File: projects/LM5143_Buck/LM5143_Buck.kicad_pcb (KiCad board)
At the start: 4 copper layers, 83 x 55 mm, 91 parts, among them J1 Bat In, J2 24V Out, J3 I2C Socket, J4 I2C Socket, Q1 IGC025S08S1, Q2 IGC025S08S1, Q3 IGC025S08S1, Q4 IGC025S08S1, SW1 Addr_Switch, SW2 Addr_Switch, U2 TLV74033, U3 INA226

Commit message: New Schematic
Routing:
- net VOUT: track 104.0 -> 0.00 mm, vias 6 -> 0
- net Net-(J3-Pin_4): track 88.7 -> 0.00 mm, vias 3 -> 0
- net Net-(J3-Pin_3): track 87.4 -> 0.00 mm, vias 3 -> 0
- net +24V: track 57.0 -> 0.00 mm, vias 57 -> 0
- net +3.3V: track 55.0 -> 0.00 mm, vias 2 -> 0
- net +5V: track 49.8 -> 0.00 mm, vias 3 -> 0
- net GNDA: track 46.5 -> 0.00 mm, vias 1 -> 0
- net Net-(U3-A1): track 35.5 -> 0.00 mm, vias 1 -> 0
- net Net-(U1-CS1): track 33.1 -> 0.00 mm, vias 2 -> 0
- net Net-(U1-CS2): track 32.9 -> 0.00 mm, vias 2 -> 0
- net /~{Alert}: track 32.1 -> 0.00 mm, vias 3 -> 0
- net PGND2: track 22.9 -> 0.00 mm, vias 2 -> 0
- net PGND1: track 19.2 -> 0.00 mm, vias 1 -> 0
- net Net-(D5-A): track 18.2 -> 0.00 mm, vias 2 -> 0
- net Net-(D3-A): track 16.4 -> 0.00 mm, vias 2 -> 0
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
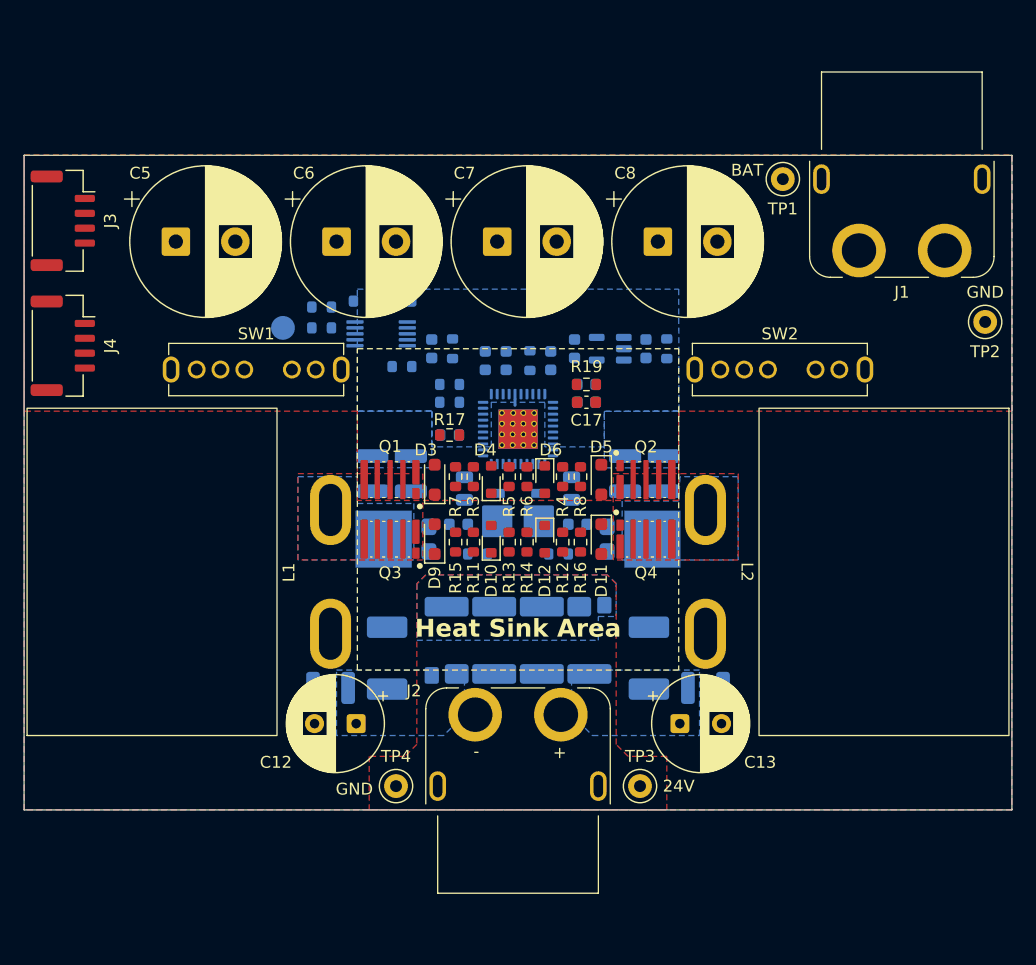
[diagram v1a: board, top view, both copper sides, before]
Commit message: Schematic update and partial routing
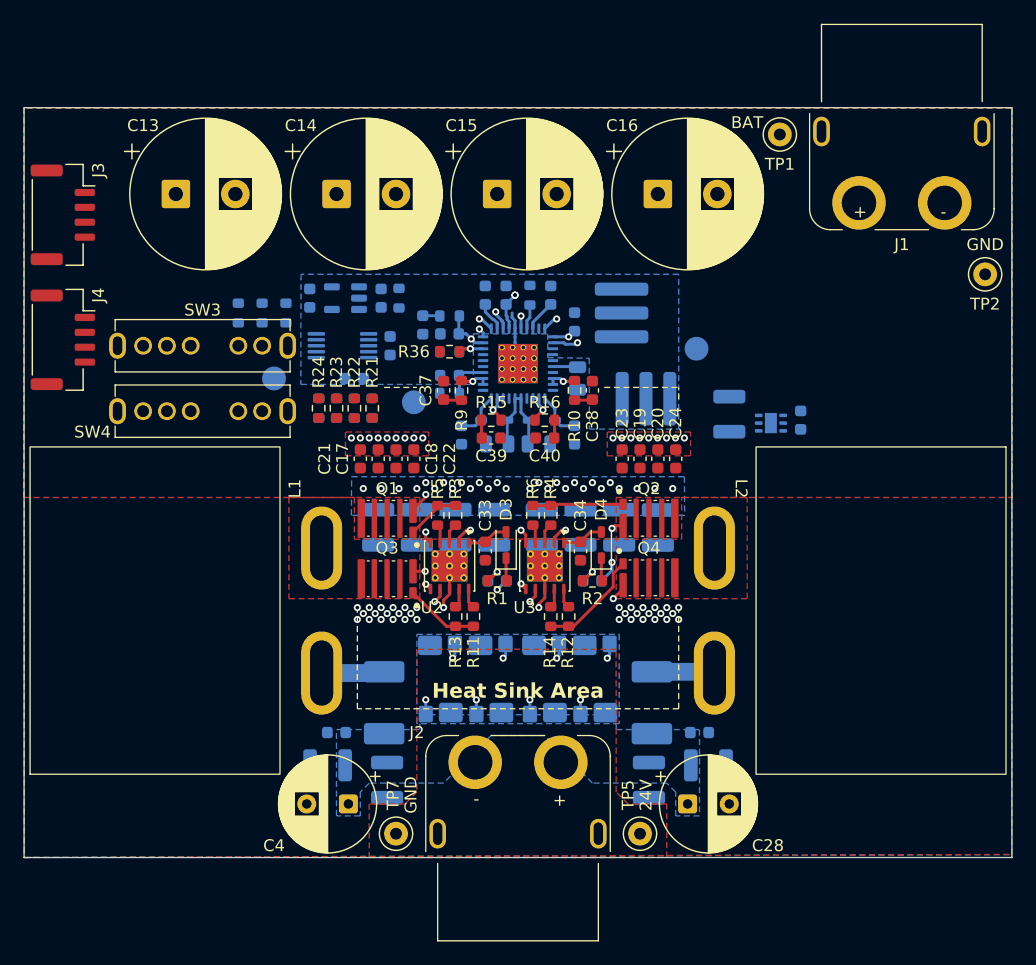
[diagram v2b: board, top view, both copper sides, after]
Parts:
- removed the C13 at (153.6, 130.2)
- removed the C14 at (155.8, 127.2)
- removed the C15 at (135.0, 113.5)
- removed the C16 at (145.0, 113.5)
- removed D10, D12, D6: PLZ5V1C, footprints:D_MicroSMF
- removed D11, D9: CUS10S30, Diode_SMD:D_SOD-323_HandSoldering
- removed D13: B18W1NG--20C000114U1930, LED_SMD:LED_0603_1608Metric
- removed D7, D8: MBR15H120PC-AU, Package_TO_SOT_SMD:TO-277A
- added C27: 100nF, Capacitor_SMD:C_0603_1608Metric, B.Cu at (155.2, 131.0)
- added C28: 100uF, Capacitor_THT:CP_Radial_D8.0mm_P3.50mm, F.Cu at (154.2, 137.0)
- added C29: 2.2uF, Capacitor_SMD:C_0805_2012Metric, B.Cu at (138.2, 106.8)
- added C30: 2.2uF, Capacitor_SMD:C_0805_2012Metric, B.Cu at (141.8, 106.8)
- added C31: 100nF, Capacitor_SMD:C_0603_1608Metric, B.Cu at (138.2, 118.2)
- added C32: 100nF, Capacitor_SMD:C_0603_1608Metric, B.Cu at (146.2, 118.2)
- added C33: 1uF, Capacitor_SMD:C_0603_1608Metric, F.Cu at (137.2, 115.8)
- added C34: 1uF, Capacitor_SMD:C_0603_1608Metric, F.Cu at (145.2, 115.8)
- added C35: 100nF, Capacitor_SMD:C_0603_1608Metric, B.Cu at (135.2, 106.0)
- added C36: 100nF, Capacitor_SMD:C_0603_1608Metric, B.Cu at (144.8, 106.0)
- added C37: 22pF, Capacitor_SMD:C_0603_1608Metric, F.Cu at (133.8, 102.2)
- added C38: 22pF, Capacitor_SMD:C_0603_1608Metric, F.Cu at (146.2, 102.2)
- added C39: 22pF, Capacitor_SMD:C_0603_1608Metric, F.Cu at (137.8, 106.2)
- added C40: 22pF, Capacitor_SMD:C_0603_1608Metric, F.Cu at (142.2, 106.2)
- added C41: 2.2uF, Capacitor_SMD:C_0805_2012Metric, B.Cu at (145.0, 101.2)
- added C42: 5.6nF, Capacitor_SMD:C_0603_1608Metric, B.Cu at (132.0, 96.8)
- added C43: 1uF, Capacitor_SMD:C_0603_1608Metric, B.Cu at (128.5, 94.5)
- added C44: 1uF, Capacitor_SMD:C_0603_1608Metric, B.Cu at (122.5, 94.5)
- added C45: 120pF, Capacitor_SMD:C_0603_1608Metric, B.Cu at (134.2, 97.5)
- added C46: 100nF, Capacitor_SMD:C_0603_1608Metric, B.Cu at (144.8, 96.5)
- added C47: 470nF, Capacitor_SMD:C_0603_1608Metric, B.Cu at (137.2, 94.2)
- added C48: 470nF, Capacitor_SMD:C_0603_1608Metric, B.Cu at (139.0, 94.2)
- added C49: 10nF, Capacitor_SMD:C_0603_1608Metric, B.Cu at (142.8, 94.2)
- added C5: 4.7uF, Capacitor_SMD:C_1210_3225Metric, B.Cu at (128.2, 113.8)
- added C50: 1uF, Capacitor_SMD:C_0603_1608Metric, B.Cu at (163.8, 104.8)
- added C51: 10uF, Capacitor_SMD:C_1210_3225Metric, B.Cu at (157.8, 104.2)
- added C52: 100nF, Capacitor_SMD:C_0603_1608Metric, B.Cu at (129.2, 98.5)
- added C53: 1uF, Capacitor_SMD:C_0603_1608Metric, B.Cu at (126.2, 101.2)
- added C6: 4.7uF, Capacitor_SMD:C_1210_3225Metric, B.Cu at (131.5, 113.8)
- added C7: 4.7uF, Capacitor_SMD:C_1210_3225Metric, B.Cu at (134.8, 113.8)
- added C8: 4.7uF, Capacitor_SMD:C_1210_3225Metric, B.Cu at (138.0, 113.8)
- added NT2: NetTie_2, footprints:NetTie-2_SMD_Pad0.25mm, F.Cu at (134.2, 118.5)
- added NT3: NetTie_2, footprints:NetTie-2_SMD_Pad0.25mm, F.Cu at (142.2, 118.5)
- added R32: 10, Resistor_SMD:R_0603_1608Metric, B.Cu at (123.2, 103.8)
- added R33: 3.3k, Resistor_SMD:R_0603_1608Metric, B.Cu at (116.5, 95.8)
- added R34: 3.3k, Resistor_SMD:R_0603_1608Metric, B.Cu at (118.5, 95.8)
- added R35: 3.3k, Resistor_SMD:R_0603_1608Metric, B.Cu at (120.5, 95.8)
- added R36: 390k, Resistor_SMD:R_0603_1608Metric, F.Cu at (134.2, 99.0)
- added R37: 10k, Resistor_SMD:R_0603_1608Metric, B.Cu at (134.2, 99.0)
- added SW1: SW_SPDT, footprints:SLW-865144-2A-N-SMT-TR, B.Cu at (149.8, 95.8)
- added SW2: SW_SPDT, footprints:SLW-865144-2A-N-SMT-TR, B.Cu at (150.8, 104.0)
- added TP6: TestPoint, TestPoint:TestPoint_Pad_D2.0mm, B.Cu at (119.5, 101.2)
- added TP7: TestPoint, TestPoint:TestPoint_Keystone_5000-5004_Miniature, F.Cu at (129.8, 139.5)
- added U4: TLV74033, Package_TO_SOT_SMD:SOT-23-5, B.Cu at (125.5, 94.5)
- added U5: AP7387-50FDC-7, Package_DFN_QFN:DFN-6-1EP_2x2mm_P0.65mm_EP1.01x1.7mm, B.Cu at (161.2, 105.0)
- added U6: INA226, Package_SO:VSSOP-10_3x3mm_P0.5mm, B.Cu at (125.2, 98.5)
- C1, C2: value 4.7uF -> 10uF
- C10, C9: value 2.2uF -> 4.7uF; footprint Capacitor_SMD:C_0805_2012Metric -> Capacitor_SMD:C_1210_3225Metric
- C11: value 10uF -> 4.7uF
- C12: value 100uF -> 4.7uF; footprint Capacitor_THT:CP_Radial_D8.0mm_P3.50mm -> Capacitor_SMD:C_1210_3225Metric; moved to B.Cu
- C17: value 3.3nF -> 10nF
- C18: value 82pF -> 10nF; moved to F.Cu
- C19: value 100nF -> 10nF; moved to F.Cu
- C20: value 470nF -> 10nF; moved to F.Cu
- C21: value 470nF -> 100nF; moved to F.Cu
- C22: value 10nF -> 100nF; moved to F.Cu
- C23, C24: value 1uF -> 100nF; moved to F.Cu
- C25: value 100nF -> 10uF; footprint Capacitor_SMD:C_0603_1608Metric -> Capacitor_SMD:C_1210_3225Metric
- C26: value 1uF -> 10uF; footprint Capacitor_SMD:C_0603_1608Metric -> Capacitor_SMD:C_1210_3225Metric
- C3: value 4.7uF -> 100nF; footprint Capacitor_SMD:C_1210_3225Metric -> Capacitor_SMD:C_0603_1608Metric
- C4: value 4.7uF -> 100uF; footprint Capacitor_SMD:C_1210_3225Metric -> Capacitor_THT:CP_Radial_D8.0mm_P3.50mm; moved to F.Cu
- D1, D2: value V2PM10L -> BAT46JFILM; footprint Diode_SMD:D_SMP_DO-220AA -> footprints:D_SOD-323_Alt
- D3: value CUS10S30 -> BAT46JFILM; footprint Diode_SMD:D_SOD-323_HandSoldering -> footprints:D_SOD-323_Alt
- D4: value PLZ5V1C -> BAT46JFILM; footprint footprints:D_MicroSMF -> footprints:D_SOD-323_Alt
- D5: value CUS10S30 -> B18W1NG--20C000114U1930; footprint Diode_SMD:D_SOD-323_HandSoldering -> LED_SMD:LED_0603_1608Metric; moved to B.Cu
- L1, L2: footprint footprints:ER26A -> footprints:CPQ2620H
- R1, R2: value 2.2 -> 100; moved to F.Cu
- R10, R9: value 2.2m -> 1k; footprint footprints:ASR2512 -> Resistor_SMD:R_0603_1608Metric; moved to F.Cu
- R11, R12, R3, R4: value 3.3 -> 2.2
- R13, R14, R5, R6: value 10k -> 1
- R15, R16: value 1 -> 1k
- R17: value 3.3k -> 100k; moved to B.Cu
- R18: value 100k -> 3.3k
- R19: value 18k -> 12k; moved to B.Cu
- R21: value 390k -> 10; moved to F.Cu
- R22: value 10k -> 10; moved to F.Cu
- R23, R24: value 3.3k -> 10; moved to F.Cu
- R25: value 3.3k -> 5m; footprint Resistor_SMD:R_0603_1608Metric -> footprints:PCSR2512
- R26: value 10 -> 5m; footprint Resistor_SMD:R_0603_1608Metric -> footprints:PCSR2512
- R27: footprint footprints:PCSR2512_Alt -> footprints:PCSR2512
- R28: footprint footprints:PCSR2512_Alt_2 -> footprints:PCSR2512
- R29: value 5m -> 10; footprint footprints:PCSR2512_Alt_2 -> Resistor_SMD:R_0603_1608Metric
- R30: value 5m -> 10; footprint footprints:PCSR2512_Alt -> Resistor_SMD:R_0603_1608Metric
- R7, R8: value 1 -> 2.2m; footprint Resistor_SMD:R_0603_1608Metric -> footprints:ASR2512; moved to B.Cu
- TP3, TP4: footprint TestPoint:TestPoint_Keystone_5000-5004_Miniature -> TestPoint:TestPoint_Pad_D2.0mm; moved to B.Cu
- TP5: footprint TestPoint:TestPoint_Pad_D2.0mm -> TestPoint:TestPoint_Keystone_5000-5004_Miniature; moved to F.Cu
- U2: value TLV74033 -> LM5113-Q1; footprint Package_TO_SOT_SMD:SOT-23-5 -> footprints:WSON-10-1EP_4x4mm_P0.8mm_EP2.6x3mm_ThermalVias; moved to F.Cu
- U3: value INA226 -> LM5113-Q1; footprint Package_SO:VSSOP-10_3x3mm_P0.5mm -> footprints:WSON-10-1EP_4x4mm_P0.8mm_EP2.6x3mm_ThermalVias; moved to F.Cu
- moved TP5 52.0 mm to (150.2, 139.5), turned to 0 degrees
- moved SW3 48.5 mm to (113.5, 97.0)
- moved C25 45.3 mm to (151.0, 135.0), turned to -90 degrees
- moved TP4 44.6 mm to (155.0, 98.8), turned to 180 degrees
- moved C26 42.0 mm to (156.0, 133.8), turned to 0 degrees
- moved C4 38.4 mm to (125.8, 137.0), turned to 180 degrees
- moved R25 38.3 mm to (148.5, 126.5), turned to 90 degrees
- moved TP3 37.4 mm to (131.2, 103.2), turned to 180 degrees
- moved C3 32.6 mm to (124.8, 131.0), turned to 180 degrees
- moved C12 30.2 mm to (151.8, 113.8), turned to 90 degrees
- moved R26 29.8 mm to (144.2, 126.5), turned to 90 degrees
- moved C11 27.8 mm to (148.5, 113.8), turned to 90 degrees
- moved C1 25.8 mm to (129.0, 135.0), turned to -90 degrees
- moved C2 25.5 mm to (124.0, 133.8), turned to 180 degrees
- moved R29 25.4 mm to (127.8, 103.8)
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- renumbered C5 to C13, C6 to C14, C7 to C15, C8 to C16, SW2 to SW3, SW1 to SW4
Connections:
- C1 pad 1: GNDPWR -> VOUT
- C1 pad 2: VDD -> GNDPWR
- C10 pad 1: +5V -> GNDPWR
- C10 pad 2: PGND2 -> VDD
- C11 pad 1: VOUT -> GNDPWR
- C11 pad 2: GNDPWR -> VDD
- C12 pad 1: VOUT -> GNDPWR
- C12 pad 2: GNDPWR -> VDD
- C17 pad 1: GNDA -> GNDPWR
- C17 pad 2: Net-(C17-Pad2) -> VDD
- C18 pad 1: GNDA -> GNDPWR
- C18 pad 2: Net-(U1-COMP1) -> VDD
- C19 pad 1: Net-(U1-SS1) -> GNDPWR
- C19 pad 2: GNDA -> VDD
- C2 pad 1: GNDPWR -> VOUT
- C2 pad 2: VDD -> GNDPWR
- C20 pad 1: Net-(U1-RES) -> GNDPWR
- C20 pad 2: GNDA -> VDD
- C21 pad 1: VDDA -> GNDPWR
- C21 pad 2: GNDA -> VDD
- C22 pad 1: Net-(U1-DITH) -> GNDPWR
- C22 pad 2: GNDA -> VDD
- C23 pad 1: +5V -> GNDPWR
- C23 pad 2: GNDA -> VDD
- C24 pad 1: +3.3V -> GNDPWR
- C24 pad 2: GNDA -> VDD
- C25 pad 1: GNDA -> VOUT
- C25 pad 2: +3.3V -> GNDPWR
- C26 pad 1: Net-(U3-Vin+) -> VOUT
- C26 pad 2: Net-(U3-Vin-) -> GNDPWR
- C3 pad 1: GNDPWR -> VOUT
- C3 pad 2: VDD -> GNDPWR
- C4 pad 1: GNDPWR -> VOUT
- C4 pad 2: VDD -> GNDPWR
- C9 pad 1: +5V -> GNDPWR
- C9 pad 2: PGND1 -> VDD
- D1 pad 2: +5V -> VCC
- D2 pad 2: +5V -> VCC
- D3 pad 2: Net-(D3-A) -> VCC
- D4 pad 1: Net-(D3-K) -> Net-(D4-K)
- D4 pad 2: Net-(D3-A) -> VCC
- D5 pad 1: Net-(D5-K) -> GNDA
- J1 pad : GNDPWR -> (no net)
- J2 pad : GNDPWR -> (no net)
- J3 pad MP: VDD -> (no net)
- J4 pad MP: VDD -> (no net)
- Q1 pad 1: Net-(D3-K) -> Net-(Q1-G)
- Q1 pad 6: Net-(D3-A) -> Net-(Q1-SS)
- Q2 pad 1: Net-(D5-K) -> Net-(Q2-G)
- Q2 pad 6: Net-(D5-A) -> Net-(Q2-SS)
- Q3 pad 1: Net-(D10-K) -> Net-(Q3-G)
- Q3 pad 6: PGND1 -> Net-(Q3-SS)
- Q4 pad 1: Net-(D11-K) -> Net-(Q4-G)
- Q4 pad 6: PGND2 -> Net-(Q4-SS)
- R1 pad 1: Net-(D1-K) -> Net-(U2-HB)
- R1 pad 2: Net-(U1-HB1) -> Net-(D3-K)
- R10 pad 1: Net-(U1-CS2) -> Net-(U3-HI)
- R10 pad 2: VOUT -> Net-(U1-HO2)
- R11 pad 1: Net-(D10-K) -> Net-(Q3-G)
- R11 pad 2: Net-(U1-LO1) -> Net-(U2-LOH)
- R12 pad 1: Net-(D11-K) -> Net-(Q4-G)
- R12 pad 2: Net-(U1-LO2) -> Net-(U3-LOH)
- R13 pad 1: Net-(D10-K) -> Net-(Q3-G)
- R13 pad 2: PGND1 -> Net-(U2-LOL)
- R14 pad 1: Net-(D11-K) -> Net-(Q4-G)
- R14 pad 2: PGND2 -> Net-(U3-LOL)
- R15 pad 1: Net-(D10-K) -> Net-(U2-LI)
- R15 pad 2: Net-(U1-LOL1) -> Net-(U1-LO1)
- R16 pad 1: Net-(D11-K) -> Net-(U3-LI)
- R16 pad 2: Net-(U1-LOL2) -> Net-(U1-LO2)
- R17 pad 1: +5V -> GNDA
- R17 pad 2: Net-(D13-A) -> Net-(U1-RT)
- R18 pad 1: GNDA -> VCC
- R18 pad 2: Net-(U1-RT) -> Net-(D5-A)
- R19 pad 1: Net-(C17-Pad2) -> Net-(C42-Pad2)
- R2 pad 1: Net-(D2-K) -> Net-(U3-HB)
- R2 pad 2: Net-(U1-HB2) -> Net-(D4-K)
- R20 pad 2: Net-(U2-EN) -> Net-(U4-EN)
- R21 pad 1: /FB1 -> Net-(R21-Pad1)
- R21 pad 2: +24V -> /R+
- R22 pad 1: GNDA -> Net-(R22-Pad1)
- R22 pad 2: /FB1 -> /R+
- R23 pad 1: +3.3V -> Net-(R23-Pad1)
- R23 pad 2: Net-(J3-Pin_3) -> /R+
- R24 pad 1: +3.3V -> Net-(R24-Pad1)
- R24 pad 2: Net-(J3-Pin_4) -> /R+
- R25 pad 1: +3.3V -> VOUT
- R25 pad 2: /~{Alert} -> Net-(R21-Pad1)
- R26 pad 2: Net-(U3-Vin+) -> Net-(R22-Pad1)
- R27 pad 1: +24V -> VOUT
- R27 pad 2: VOUT -> Net-(R23-Pad1)
- R28 pad 2: +24V -> Net-(R24-Pad1)
- R29 pad 1: VOUT -> Net-(R25-Pad3)
- R29 pad 2: +24V -> /R-
- R3 pad 1: Net-(D3-K) -> Net-(Q1-G)
- R3 pad 2: Net-(U1-HO1) -> Net-(U2-HOH)
- R30 pad 1: VOUT -> Net-(R26-Pad3)
- R30 pad 2: +24V -> /R-
- R31 pad 1: +24V -> Net-(R27-Pad3)
- R31 pad 2: Net-(U3-Vin-) -> /R-
- R4 pad 1: Net-(D5-K) -> Net-(Q2-G)
- R4 pad 2: Net-(U1-HO2) -> Net-(U3-HOH)
- R5 pad 1: Net-(D3-K) -> Net-(Q1-G)
- R5 pad 2: Net-(D3-A) -> Net-(U2-HOL)
- R6 pad 1: Net-(D5-K) -> Net-(Q2-G)
- R6 pad 2: Net-(D5-A) -> Net-(U3-HOL)
- R7 pad 1: Net-(D3-K) -> Net-(U1-CS1)
- R7 pad 2: Net-(U1-HOL1) -> VOUT
- R8 pad 1: Net-(D5-K) -> Net-(U1-CS2)
- R8 pad 2: Net-(U1-HOL2) -> VOUT
- R9 pad 1: Net-(U1-CS1) -> Net-(U2-HI)
- R9 pad 2: VOUT -> Net-(U1-HO1)
- SW3 pad : GNDPWR -> (no net)
- SW3 pad 5: Net-(U3-A1) -> Net-(U6-A1)
- SW4 pad : GNDPWR -> (no net)
- SW4 pad 5: Net-(U3-A0) -> Net-(U6-A0)
- TP3 pad 1: +24V -> VCC
- TP4 pad 1: GNDPWR -> Net-(SW2-B)
- TP5 pad 1: /~{Alert} -> +24V
- U1 pad 10: Net-(D5-A) -> GNDPWR
- U1 pad 11: Net-(U1-HB2) -> Net-(D2-K)
- U1 pad 12: Net-(U1-LOL2) -> Net-(U1-LO2)
- U1 pad 14: PGND2 -> GNDPWR
- U1 pad 15: +5V -> VCC
- U1 pad 16: +5V -> VCC
- U1 pad 17: PGND1 -> GNDPWR
- U1 pad 19: Net-(U1-LOL1) -> Net-(U1-LO1)
- U1 pad 20: Net-(U1-HB1) -> Net-(D1-K)
- U1 pad 21: Net-(D3-A) -> GNDPWR
- U1 pad 23: Net-(U1-HOL1) -> Net-(U1-HO1)
- U1 pad 24: Net-(D13-A) -> Net-(D5-A)
- U1 pad 33: GNDA -> Net-(SW1-B)
- U1 pad 6: GNDA -> Net-(SW2-B)
- U1 pad 8: Net-(U1-HOL2) -> Net-(U1-HO2)
- U2 pad 1: +5V -> VCC
- U2 pad 2: GNDA -> Net-(U2-HB)
- U2 pad 3: Net-(U2-EN) -> Net-(U2-HOH)
- U2 pad 4: unconnected-(U2-NC-Pad4) -> Net-(U2-HOL)
- U2 pad 5: +3.3V -> Net-(Q1-SS)
- U3 pad 1: Net-(U3-A1) -> VCC
- U3 pad 10: Net-(U3-Vin+) -> Net-(U3-LOH)
- U3 pad 2: Net-(U3-A0) -> Net-(U3-HB)
- U3 pad 3: /~{Alert} -> Net-(U3-HOH)
- U3 pad 4: Net-(J3-Pin_3) -> Net-(U3-HOL)
- U3 pad 5: Net-(J3-Pin_4) -> Net-(Q2-SS)
- U3 pad 6: +3.3V -> Net-(U3-HI)
- U3 pad 7: GNDA -> Net-(U3-LI)
- U3 pad 8: +24V -> Net-(Q4-SS)
- U3 pad 9: Net-(U3-Vin-) -> Net-(U3-LOL)
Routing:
- net Net-(Q1-SS): track 0.00 -> 15.9 mm, vias 0 -> 3
- net VCC: track 0.00 -> 15.8 mm
- net Net-(U1-COMP1): track 0.00 -> 15.2 mm, vias 0 -> 2
- net Net-(Q2-SS): track 0.00 -> 15.1 mm, vias 0 -> 3
- net Net-(U1-SS1): track 0.00 -> 10.6 mm, vias 0 -> 2
- net Net-(Q4-SS): track 0.00 -> 9.80 mm, vias 0 -> 2
- net /~{Alert}: track 0.00 -> 9.65 mm, vias 0 -> 2
- net Net-(Q4-G): track 0.00 -> 8.89 mm
- net Net-(U3-HB): track 0.00 -> 8.30 mm, vias 0 -> 2
- net Net-(U2-HB): track 0.00 -> 8.30 mm, vias 0 -> 2
- net Net-(Q3-SS): track 0.00 -> 7.84 mm, vias 0 -> 2
- net Net-(Q2-G): track 0.00 -> 7.62 mm
- net VDDA: track 0.00 -> 6.25 mm, vias 0 -> 3
- net Net-(Q3-G): track 0.00 -> 6.24 mm
- net Net-(U1-CS2): track 0.00 -> 5.29 mm
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- removed copper zone on B.Cu, net Net-(L1-Pad2)
- removed copper zone on B.Cu, net Net-(L2-Pad1)
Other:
- board size 83 x 55 mm -> 83 x 63 mm
- board text added: "(VCC)"
- board text added: "(VCCX)"
- board text added: "(~{Alert})"
- board text removed: "~{Alert}"

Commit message: Fully routed, no via stitching yet
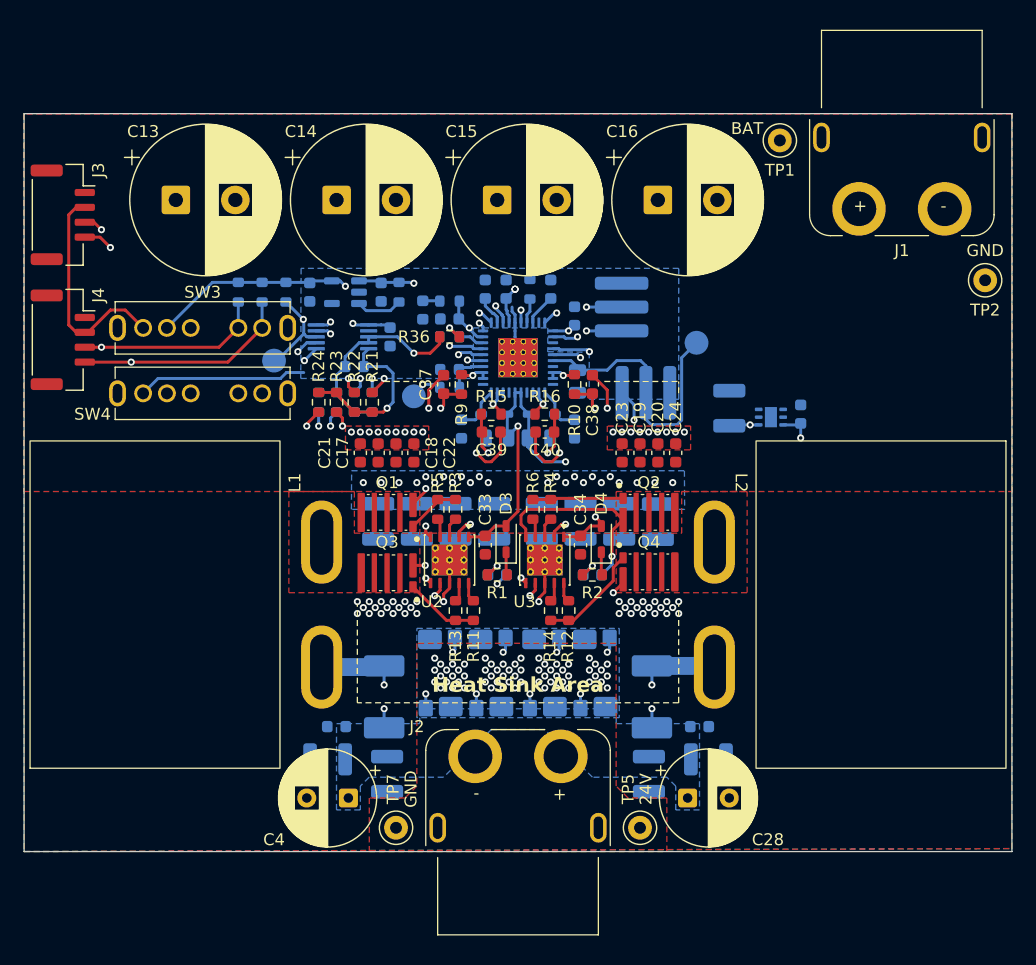
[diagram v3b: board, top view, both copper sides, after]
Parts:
- moved SW3 7.00 mm to (113.5, 95.5)
- moved SW4 4.00 mm to (113.5, 101.0)
- moved R33 1.75 mm to (116.5, 94.0)
- moved R34 1.75 mm to (118.5, 94.0)
- moved R35 1.75 mm to (120.5, 94.0)
- moved TP6 1.50 mm to (119.5, 99.8)
- moved C42 1.25 mm to (132.0, 95.5)
- moved C45 1.25 mm to (134.2, 96.2)
- moved R19 1.25 mm to (134.2, 94.8)
- moved R36 1.25 mm to (134.2, 97.8)
- moved R37 1.25 mm to (134.2, 97.8)
- moved C53 1.00 mm to (126.2, 100.2)
- moved C52 0.75 mm to (129.2, 97.8)
- moved U6 0.75 mm to (125.2, 97.8)
- moved C1 0.50 mm to (129.0, 134.5)
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- renumbered SW4 to SW3, SW3 to SW4
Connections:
- J1 pad : (no net) -> GNDPWR
- J3 pad MP: (no net) -> VDD
- J4 pad MP: (no net) -> VDD
- R36 pad 2: +24V -> /R-
- SW3 pad : (no net) -> GNDPWR
- SW4 pad : (no net) -> GNDPWR
- U6 pad 8: +24V -> /R-
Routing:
- net VOUT: track 0.00 -> 107.1 mm, vias 0 -> 4
- net Net-(U1-CS1): track 5.29 -> 57.9 mm, vias 0 -> 2
- net Net-(U1-CS2): track 5.29 -> 55.4 mm, vias 0 -> 2
- net Net-(J3-Pin_4): track 0.00 -> 44.7 mm, vias 0 -> 3
- net +5V: track 0.00 -> 44.3 mm, vias 0 -> 3
- net Net-(J3-Pin_3): track 0.00 -> 42.9 mm, vias 0 -> 3
- net Net-(R24-Pad1): track 1.20 -> 41.4 mm, vias 1 -> 2
- net Net-(R22-Pad1): track 1.20 -> 40.9 mm, vias 1 -> 2
- net Net-(R21-Pad1): track 1.20 -> 40.7 mm, vias 1 -> 2
- net Net-(R25-Pad3): track 1.28 -> 40.6 mm, vias 1 -> 2
- net GNDA: track 2.10 -> 40.6 mm
- net VCC: track 15.8 -> 53.6 mm, vias 0 -> 4
- net Net-(R23-Pad1): track 1.20 -> 38.7 mm, vias 1 -> 2
- net Net-(R26-Pad3): track 1.28 -> 38.1 mm, vias 1 -> 2
- net Net-(R28-Pad3): track 1.28 -> 36.6 mm, vias 1 -> 2
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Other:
- board size 83 x 63 mm -> 83 x 62 mm

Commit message: Added more capacitors
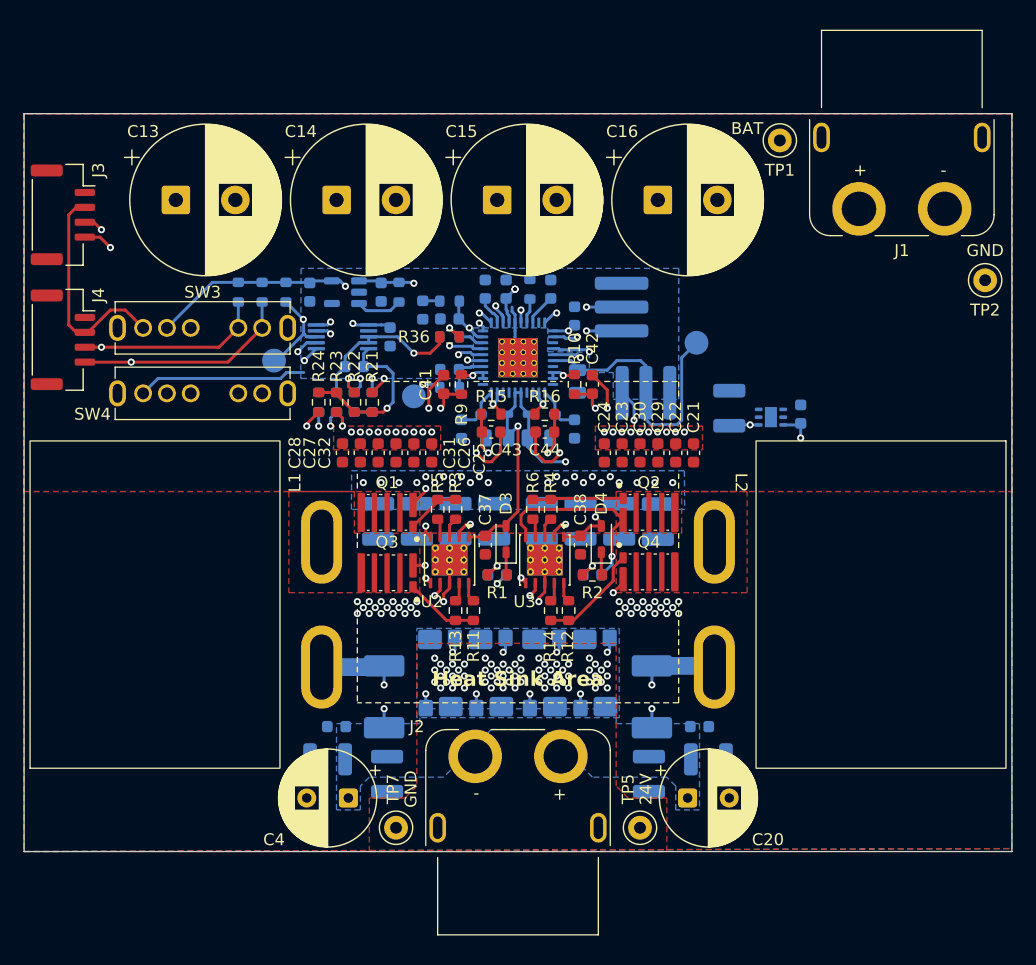
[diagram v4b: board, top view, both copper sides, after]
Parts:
- added C21: 100nF, Capacitor_SMD:C_0603_1608Metric, F.Cu at (154.8, 107.5)
- added C22: 100nF, Capacitor_SMD:C_0603_1608Metric, F.Cu at (153.2, 107.5)
- added C23: 100nF, Capacitor_SMD:C_0603_1608Metric, F.Cu at (148.8, 107.5)
- added C24: 100nF, Capacitor_SMD:C_0603_1608Metric, F.Cu at (147.2, 107.5)
- moved C25 20.5 mm to (132.8, 107.5)
- moved C26 17.5 mm to (131.2, 107.5)
- moved C27 4.50 mm to (126.8, 107.5)
- moved C28 1.50 mm to (125.2, 107.5)
- renumbered C25 to C17, C26 to C18, C27 to C19, C28 to C20, C24 to C25, C23 to C26, C22 to C27, C21 to C28, C20 to C29, C19 to C30, C18 to C31, C17 to C32, C29 to C33, C30 to C34, C31 to C35, C32 to C36, C33 to C37, C34 to C38, C35 to C39, C36 to C40, C37 to C41, C38 to C42, C39 to C43, C40 to C44, C41 to C45, C42 to C46, C43 to C47, C44 to C48, C45 to C49, C46 to C50, C47 to C51, C48 to C52, C49 to C53, C50 to C54, C51 to C55, C52 to C56, C53 to C57
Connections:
- J1 pad : GNDPWR -> (no net)
- J3 pad MP: VDD -> (no net)
- J4 pad MP: VDD -> (no net)
- SW3 pad : GNDPWR -> (no net)
- SW4 pad : GNDPWR -> (no net)
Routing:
- net GNDPWR: vias 56 -> 58

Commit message: Add via stitching
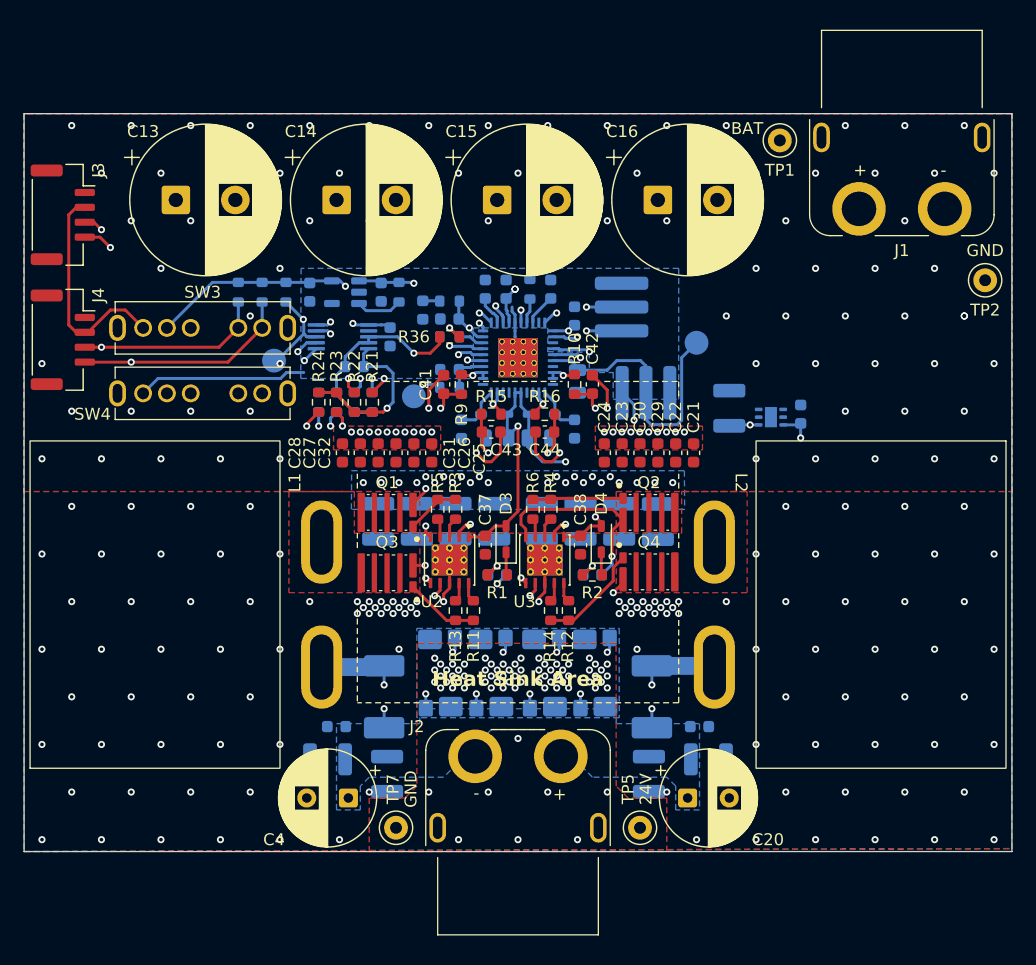
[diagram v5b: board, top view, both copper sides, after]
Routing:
- net GNDPWR: vias 58 -> 229
